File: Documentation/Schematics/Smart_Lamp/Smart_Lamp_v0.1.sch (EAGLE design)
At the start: 7 parts, among them IC1 DS3231/SO

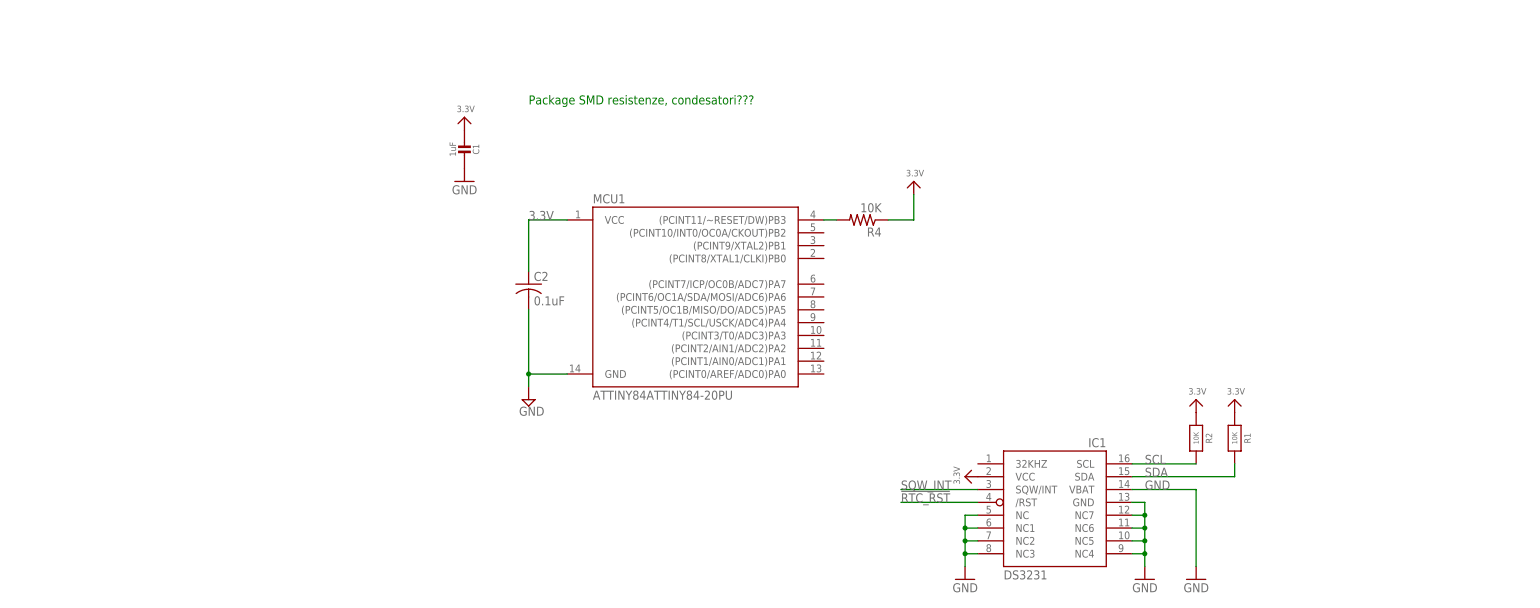
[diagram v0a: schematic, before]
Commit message: Added regulator and bluetooth module to schematic
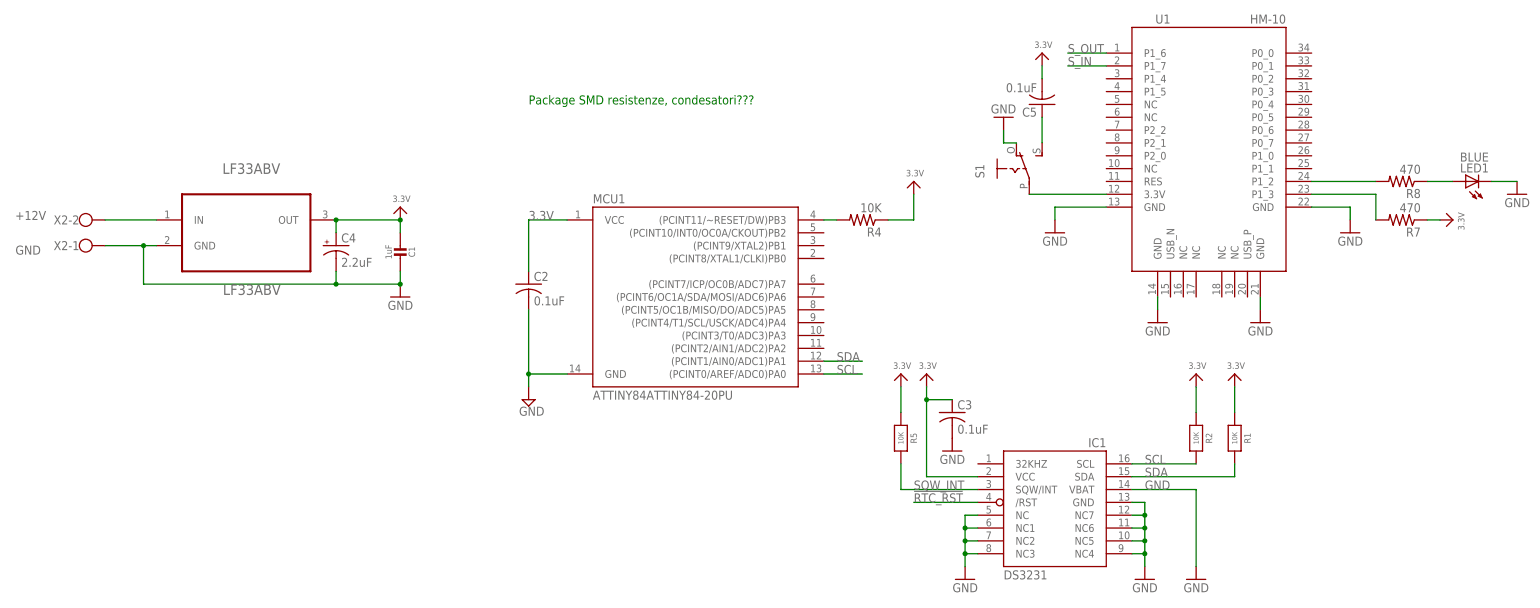
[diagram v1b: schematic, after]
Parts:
- added C3: 0.1uF, adafruit:C-USC0805
- added C4: 2.2uF, SparkFun-Capacitors:CAP_POLPTH2
- added C5: 0.1uF, adafruit:C-US025-024X044
- added LED1: BLUE, adafruit:LED3MM
- added LF33ABV: LF33ABV, ST Microelctronics_By_element14_Batch_1:LF33ABV
- added R5: 10K, microbuilder:RESISTOR0805_NOOUTLINE
- added R7, R8: 470, rcl:R-US_0207/10
- added S1: (no value), adafruit:EG1218S
- added U1: HM-10, HM-10_BLE:HM-10
- added X2: (no value), con-wago-500:W237-102
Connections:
- new net +12V: LF33ABV.IN, X2-2.KL
- new net N$1: S1.P, U1.3.3V
- new net N$10: LED1.A, R8.1
- new net N$12: R7.2, U1.P1_3
- new net N$2: C5.1, S1.S
- new net N$9: R8.2, U1.P1_2
- new net S_IN: U1.P1_7
- new net S_OUT: U1.P1_6
- net 3.3V: now also C3.1, C4.+, C5.2, LF33ABV.OUT, R5.1, R7.1
- net GND: now also C3.2, C4.-, LED1.C, LF33ABV.GND, S1.O, U1.GND@1, U1.GND@2, U1.GND@3, U1.GND@4, X2-1.KL
- net SCL: now also MCU1.(PCINT0/AREF/ADC0)PA0
- net SDA: now also MCU1.(PCINT1/AIN0/ADC1)PA1
- net SQW_INT: now also R5.2
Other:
- moved on the sheet: C1

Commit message: Small changes to schematic
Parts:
- R7: value 470 -> 1K
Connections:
- net 3.3V: now also C5.1; no longer C5.2
- net N$2: now also C5.2; no longer C5.1
- net S_IN: now also MCU1.(PCINT2/AIN1/ADC2)PA2
- net S_OUT: now also MCU1.(PCINT3/T0/ADC3)PA3
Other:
- moved on the sheet: C5
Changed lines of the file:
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@@
 <part name="X2" library="con-wago-500" deviceset="W237-102" device=""/>
 <part name="U1" library="HM-10_BLE" deviceset="HM-10" device=""/>
-<part name="R7" library="rcl" deviceset="R-US_" device="0207/10" value="470"/>
+<part name="R7" library="rcl" deviceset="R-US_" device="0207/10" value="1K"/>
 <part name="R8" library="rcl" deviceset="R-US_" device="0207/10" value="470"/>
 <part name="LED1" library="adafruit" deviceset="LED" device="3MM" value="BLUE"/>
@@
 <instance part="R8" gate="G$1" x="187.96" y="88.9" rot="R180"/>
 <instance part="LED1" gate="G$1" x="200.66" y="88.9" rot="R90"/>
-<instance part="U$7" gate="G$1" x="116.84" y="114.3"/>
+<instance part="U$7" gate="G$1" x="116.84" y="111.76"/>
 <instance part="GND7" gate="1" x="119.38" y="78.74" rot="MR0"/>
 <instance part="GND8" gate="1" x="139.7" y="60.96" rot="MR0"/>
@@
 <instance part="GND12" gate="1" x="210.82" y="86.36" rot="MR0"/>
 <instance part="U$8" gate="G$1" x="198.12" y="81.28" rot="R270"/>
-<instance part="C5" gate="G$1" x="116.84" y="104.14" rot="R180"/>
+<instance part="C5" gate="G$1" x="116.84" y="104.14"/>
 <instance part="S1" gate="1" x="111.76" y="91.44"/>
 <instance part="GND6" gate="1" x="109.22" y="101.6" rot="MR180"/>
@@
 </segment>
 <segment>
-<pinref part="C5" gate="G$1" pin="2"/>
 <pinref part="U$7" gate="G$1" pin="3.3V"/>
-<wire x1="116.84" y1="109.22" x2="116.84" y2="111.76" width="0.1524" layer="91"/>
+<pinref part="C5" gate="G$1" pin="1"/>
+<wire x1="116.84" y1="109.22" x2="116.84" y2="106.68" width="0.1524" layer="91"/>
 </segment>
 </net>
@@
 <label x="121.92" y="114.3" size="1.778" layer="95"/>
 </segment>
+<segment>
+<pinref part="MCU1" gate="G$1" pin="(PCINT3/T0/ADC3)PA3"/>
+<wire x1="73.66" y1="58.42" x2="81.28" y2="58.42" width="0.1524" layer="91"/>
+<label x="76.2" y="58.42" size="1.778" layer="95"/>
+</segment>
 </net>
 <net name="S_IN" class="0">
@@
 <wire x1="129.54" y1="111.76" x2="121.92" y2="111.76" width="0.1524" layer="91"/>
 <label x="121.92" y="111.76" size="1.778" layer="95"/>
+</segment>
+<segment>
+<pinref part="MCU1" gate="G$1" pin="(PCINT2/AIN1/ADC2)PA2"/>
+<wire x1="73.66" y1="55.88" x2="81.28" y2="55.88" width="0.1524" layer="91"/>
+<label x="76.2" y="55.88" size="1.778" layer="95"/>
 </segment>
 </net>
@@
 <net name="N$2" class="0">
 <segment>
+<pinref part="C5" gate="G$1" pin="2"/>
 <pinref part="S1" gate="1" pin="S"/>
-<pinref part="C5" gate="G$1" pin="1"/>
-<wire x1="116.84" y1="96.52" x2="116.84" y2="101.6" width="0.1524" layer="91"/>
-</segment>
-</net>
+<wire x1="116.84" y1="99.06" x2="116.84" y2="96.52" width="0.1524" layer="91"/>
+</segment>
+</net>
